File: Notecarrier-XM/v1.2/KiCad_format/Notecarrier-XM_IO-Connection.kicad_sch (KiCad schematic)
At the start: 7 parts, among them P1 Header Castellated 2.54mm 1X16, P2 Header Castellated 2.54mm 1X16, P3 12402012E212A

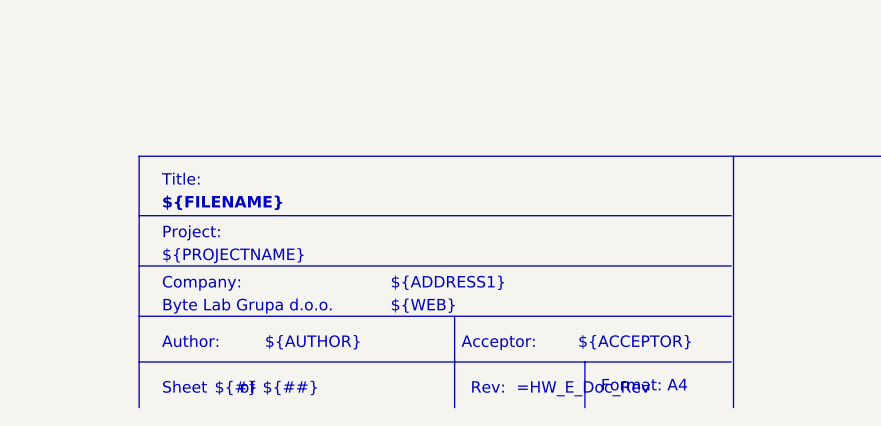
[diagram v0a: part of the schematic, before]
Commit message: Notecarrier CX/X/XS/XM: remove the Altium sheet template's dead title block
Each sheet on these four boards carried the Altium sheet template's title block
imported as 19 literal graphic text items - "Title:", "Project:", "Company:" and
friends, plus Altium's never-resolved ${PROJECTNAME}/${AUTHOR}/${ACCEPTOR}/
${ADDRESS1}/${WEB} placeholders. They render as white text printed over KiCad's
own title block, which carries the real metadata. The XI, Cygnet, Scoop and Mojo
ports had this cleaned during porting; these four did not, and it showed as
doubled, garbled text in the bottom-right of every published schematic render.

Removed all 266 items (19 per sheet, 14 sheets) with a rule requiring both the
known template string AND a position below y=170mm - real sheet content never
reaches past y=166.8 on any of these sheets, and the template cluster starts at
y=180. Graphical text only: each board's exported netlist is identical before
and after, and the committed kicanvas screenshots are regenerated (all four
boards PASS).

Found while publishing these schematics to blues.dev, where the doubled title
block was the most visible defect on every sheet.

Co-Authored-By: Claude Fable 5 <noreply@anthropic.com>
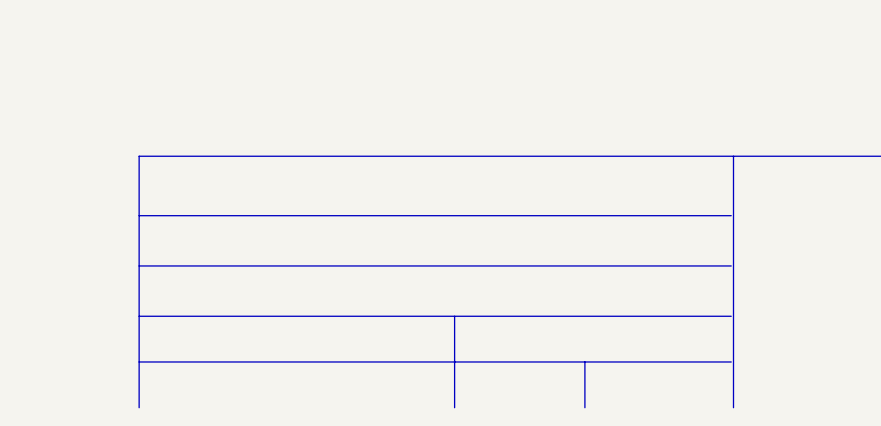
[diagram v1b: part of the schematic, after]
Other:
- note removed: "${##}"
- note removed: "${#}"
- note removed: "${ACCEPTOR}"
- note removed: "${ADDRESS1}"
- note removed: "${AUTHOR}"
- note removed: "${COMPANY}"
- note removed: "${FILENAME}"
- note removed: "${PROJECTNAME}"
- note removed: "${REVISION}"
- note removed: "${WEB}"
- note removed: "Acceptor:"
- note removed: "Author:"
- note removed: "Company:"
- note removed: "Format: A4"
- note removed: "Project:"
- note removed: "Rev:"
- note removed: "Sheet"
- note removed: "Title:"
- note removed: "of"
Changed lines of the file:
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@@
 		(company "Byte Lab Grupa d.o.o.")
-	)
-	(text "${##}"
-		(exclude_from_sim no)
-		(at 206.756 203.6572 0)
-		(effects
-			(font
-				(size 1.27 1.27)
-			)
-			(justify left bottom)
-		)
-	)
-	(text "Company:"
-		(exclude_from_sim no)
-		(at 195.58 191.9732 0)
-		(effects
-			(font
-				(size 1.27 1.27)
-			)
-			(justify left bottom)
-		)
-	)
-	(text "Format: A4"
-		(exclude_from_sim no)
-		(at 244.348 203.4032 0)
-		(effects
-			(font
-				(size 1.27 1.27)
-			)
-			(justify left bottom)
-		)
-	)
-	(text "Acceptor:"
-		(exclude_from_sim no)
-		(at 228.854 198.5772 0)
-		(effects
-			(font
-				(size 1.27 1.27)
-			)
-			(justify left bottom)
-		)
-	)
-	(text "Title:"
-		(exclude_from_sim no)
-		(at 195.58 180.5432 0)
-		(effects
-			(font
-				(size 1.27 1.27)
-			)
-			(justify left bottom)
-		)
-	)
-	(text "${ACCEPTOR}"
-		(exclude_from_sim no)
-		(at 241.808 198.5772 0)
-		(effects
-			(font
-				(size 1.27 1.27)
-			)
-			(justify left bottom)
-		)
-	)
-	(text "${AUTHOR}"
-		(exclude_from_sim no)
-		(at 207.01 198.5772 0)
-		(effects
-			(font
-				(size 1.27 1.27)
-			)
-			(justify left bottom)
-		)
 	)
 	(text "I/O Pin Headers & Castellations"
@@
 				(thickness 0.508)
 				(bold yes)
-			)
-			(justify left bottom)
-		)
-	)
-	(text "${PROJECTNAME}"
-		(exclude_from_sim no)
-		(at 195.58 188.9252 0)
-		(effects
-			(font
-				(size 1.27 1.27)
-			)
-			(justify left bottom)
-		)
-	)
-	(text "Project:"
-		(exclude_from_sim no)
-		(at 195.58 186.3852 0)
-		(effects
-			(font
-				(size 1.27 1.27)
 			)
 			(justify left bottom)
@@
 		)
 	)
-	(text "of"
-		(exclude_from_sim no)
-		(at 204.216 203.6572 0)
-		(effects
-			(font
-				(size 1.27 1.27)
-			)
-			(justify left bottom)
-		)
-	)
-	(text "${REVISION}"
-		(exclude_from_sim no)
-		(at 234.95 203.6572 0)
-		(effects
-			(font
-				(size 1.27 1.27)
-			)
-			(justify left bottom)
-		)
-	)
-	(text "Author:"
-		(exclude_from_sim no)
-		(at 195.58 198.5772 0)
-		(effects
-			(font
-				(size 1.27 1.27)
-			)
-			(justify left bottom)
-		)
-	)
-	(text "${COMPANY}"
-		(exclude_from_sim no)
-		(at 195.58 194.5132 0)
-		(effects
-			(font
-				(size 1.27 1.27)
-			)
-			(justify left bottom)
-		)
-	)
-	(text "Rev:"
-		(exclude_from_sim no)
-		(at 229.87 203.6572 0)
-		(effects
-			(font
-				(size 1.27 1.27)
-			)
-			(justify left bottom)
-		)
-	)
 	(text "Copyright © 2023 Blues Inc."
 		(exclude_from_sim no)
@@
 		(effects
 			(font
-				(size 1.27 1.27)
-			)
-			(justify left bottom)
-		)
-	)
-	(text "Sheet"
-		(exclude_from_sim no)
-		(at 195.58 203.6572 0)
-		(effects
-			(font
-				(size 1.27 1.27)
-			)
-			(justify left bottom)
-		)
-	)
-	(text "${#}"
-		(exclude_from_sim no)
-		(at 201.422 203.6572 0)
-		(effects
-			(font
-				(size 1.27 1.27)
-			)
-			(justify left bottom)
-		)
-	)
-	(text "${FILENAME}"
-		(exclude_from_sim no)
-		(at 195.58 183.0832 0)
-		(effects
-			(font
-				(size 1.27 1.27)
-				(thickness 0.254)
-				(bold yes)
-			)
-			(justify left bottom)
-		)
-	)
-	(text "${WEB}"
-		(exclude_from_sim no)
-		(at 220.98 194.5132 0)
-		(effects
-			(font
-				(size 1.27 1.27)
-			)
-			(justify left bottom)
-		)
-	)
-	(text "${ADDRESS1}"
-		(exclude_from_sim no)
-		(at 220.98 191.9732 0)
-		(effects
-			(font
